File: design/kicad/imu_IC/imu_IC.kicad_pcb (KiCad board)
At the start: 2 copper layers, 26 x 20 mm, 9 parts, among them J1 Conn_01x04, J2 Conn_01x04, U1 ISM330DHCX

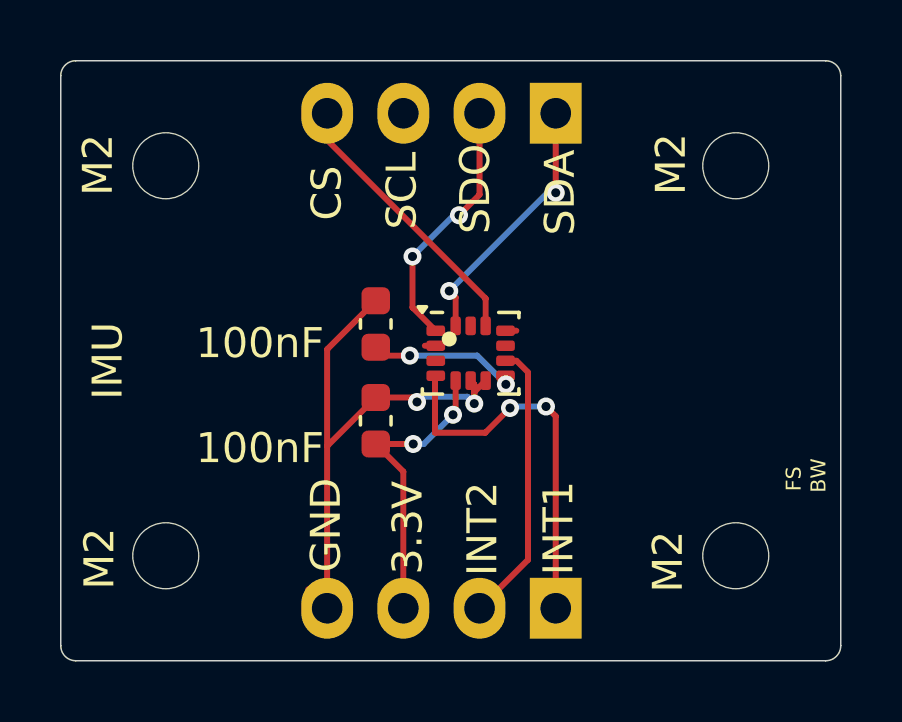
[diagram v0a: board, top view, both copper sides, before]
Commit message: File restructure, IMU PCB updated
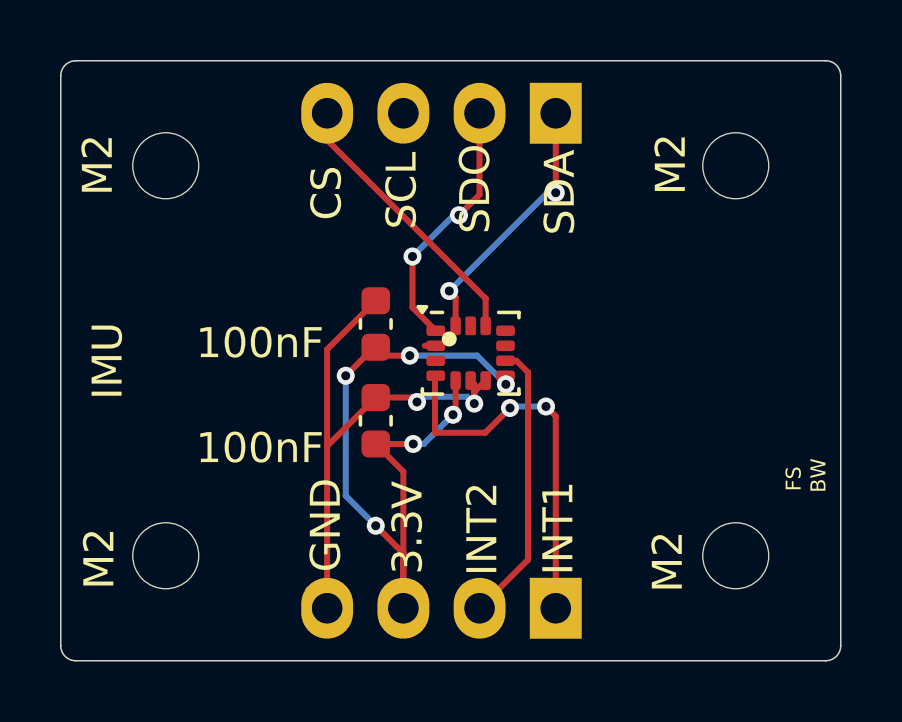
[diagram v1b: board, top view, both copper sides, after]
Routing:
- net +3.3V: track 15.2 -> 25.1 mm, vias 4 -> 6
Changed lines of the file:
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@@
 			(size 0.35 0.625)
 			(layers "F.Cu" "F.Paste" "F.Mask")
-			(roundrect_rratio 0.25)
+			(roundrect_rratio 0.15)
 			(net 11 "unconnected-(U1-SCL-Pad13)")
 			(pinfunction "SCL")
@@
 	)
 	(segment
+		(start 134.95 79.05)
+		(end 134 80)
+		(width 0.2)
+		(layer "F.Cu")
+		(net 1)
+	)
+	(segment
 		(start 135.92 87.75)
 		(end 135.92 83.195)
@@
 	)
 	(segment
+		(start 135 79.05)
+		(end 134.95 79.05)
+		(width 0.2)
+		(layer "F.Cu")
+		(net 1)
+	)
+	(segment
 		(start 139.325 80)
 		(end 139.325 80.274405)
@@
 	)
 	(segment
+		(start 135 85)
+		(end 135.92 85.92)
+		(width 0.2)
+		(layer "F.Cu")
+		(net 1)
+	)
+	(segment
 		(start 137.6625 81.2125)
 		(end 137.6625 80.1625)
+		(width 0.2)
+		(layer "F.Cu")
+		(net 1)
+	)
+	(segment
+		(start 135.92 85.92)
+		(end 135.92 87.75)
 		(width 0.2)
 		(layer "F.Cu")
@@
 	)
 	(via
+		(at 135 85)
+		(size 0.6)
+		(drill 0.3)
+		(layers "F.Cu" "B.Cu")
+		(net 1)
+	)
+	(via
 		(at 136.135259 79.32892)
 		(size 0.6)
@@
 	)
 	(via
+		(at 134 80)
+		(size 0.6)
+		(drill 0.3)
+		(layers "F.Cu" "B.Cu")
+		(net 1)
+	)
+	(via
 		(at 136.25 82.275)
 		(size 0.6)
@@
 	)
 	(segment
+		(start 134 80)
+		(end 134 84)
+		(width 0.2)
+		(layer "B.Cu")
+		(net 1)
+	)
+	(segment
 		(start 138.379515 79.32892)
 		(end 136.135259 79.32892)
@@
 		(start 139.3375 80.286905)
 		(end 138.379515 79.32892)
+		(width 0.2)
+		(layer "B.Cu")
+		(net 1)
+	)
+	(segment
+		(start 134 84)
+		(end 135 85)
 		(width 0.2)
 		(layer "B.Cu")
@@
 	)
 	(segment
-		(start 139.687932 78.5)
-		(end 139.325 78.5)
-		(width 0.2)
-		(layer "F.Cu")
-		(net 9)
-	)
-	(segment
